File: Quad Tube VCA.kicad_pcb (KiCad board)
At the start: 2 copper layers, 162.6 x 100.3 mm, 226 parts, among them IC1 TL072, IC10 TL072, IC2 LM358, IC3 TL072, IC4 LM358, IC5 TL072, IC6 LM358, IC7 TL072, IC8 LM358, IC9 TL072

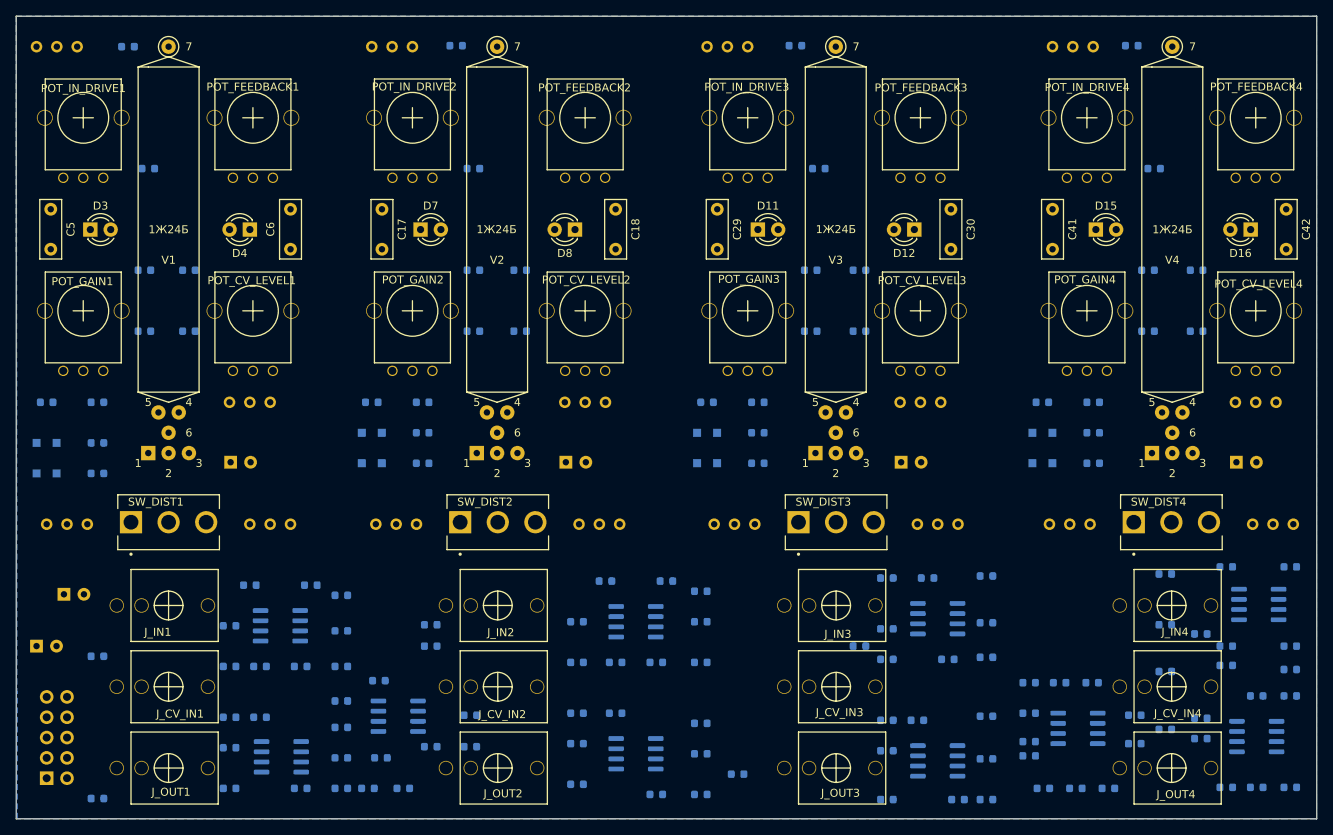
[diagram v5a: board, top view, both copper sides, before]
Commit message: first GND pour
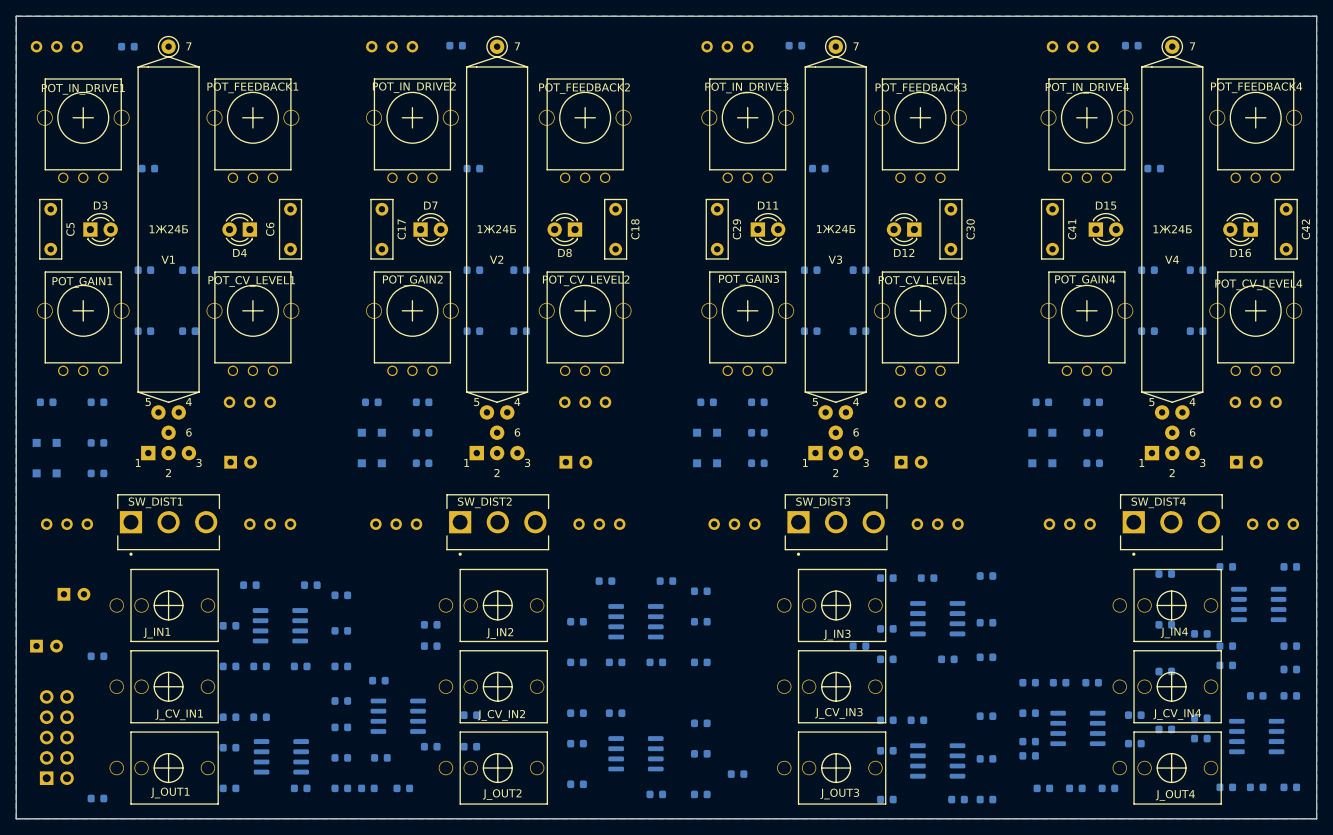
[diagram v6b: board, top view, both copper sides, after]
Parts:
- turned C16 to 180 degrees
- turned C46 to 180 degrees
- turned FB1 to 0 degrees
- turned R1 to 180 degrees
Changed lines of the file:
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@@
     (pad_to_mask_clearance 0.05)
     (aux_axis_origin 0 0)
-    (visible_elements FEFFF7FF)
+    (visible_elements FEFFFFFF)
     (pcbplotparams
       (layerselection 0x010fc_ffffffff)
@@
   )
   (module Resistor_SMD:R_0603_1608Metric (layer B.Cu)
-    (at 106.68 133.35)
+    (at 106.68 133.35 180)
     (descr "Resistor SMD 0603 (1608 Metric), square (rectangular) end terminal, IPC_7351 nominal, (Body size source: http://www.tortai-tech.com/upload/download/2011102023233369053.pdf), generated with kicad-footprint-generator")
     (tags resistor)
@@
       (effects (font (size 0.4 0.4) (thickness 0.06)) (justify mirror))
     )
-    (pad 2 smd roundrect (at 0.7875 0) (size 0.875 0.95) (layers B.Cu B.Paste B.Mask) (roundrect_rratio 0.25)
+    (pad 2 smd roundrect (at 0.7875 0 180) (size 0.875 0.95) (layers B.Cu B.Paste B.Mask) (roundrect_rratio 0.25)
       (net 81 "Net-(POT_FEEDBACK1-Pad1)"))
-    (pad 1 smd roundrect (at -0.7875 0) (size 0.875 0.95) (layers B.Cu B.Paste B.Mask) (roundrect_rratio 0.25)
+    (pad 1 smd roundrect (at -0.7875 0 180) (size 0.875 0.95) (layers B.Cu B.Paste B.Mask) (roundrect_rratio 0.25)
       (net 6 "Net-(C4-Pad2)"))
     (model ${KISYS3DMOD}/Resistor_SMD.3dshapes/R_0603_1608Metric.wrl
@@
   )
   (module Resistor_SMD:R_0603_1608Metric (layer B.Cu)
-    (at 76.2 142.24 180)
+    (at 76.2 142.24)
     (descr "Resistor SMD 0603 (1608 Metric), square (rectangular) end terminal, IPC_7351 nominal, (Body size source: http://www.tortai-tech.com/upload/download/2011102023233369053.pdf), generated with kicad-footprint-generator")
     (tags resistor)
@@
       (effects (font (size 0.4 0.4) (thickness 0.06)) (justify mirror))
     )
-    (pad 2 smd roundrect (at 0.7875 0 180) (size 0.875 0.95) (layers B.Cu B.Paste B.Mask) (roundrect_rratio 0.25)
+    (pad 2 smd roundrect (at 0.7875 0) (size 0.875 0.95) (layers B.Cu B.Paste B.Mask) (roundrect_rratio 0.25)
       (net 4 +12V))
-    (pad 1 smd roundrect (at -0.7875 0 180) (size 0.875 0.95) (layers B.Cu B.Paste B.Mask) (roundrect_rratio 0.25)
+    (pad 1 smd roundrect (at -0.7875 0) (size 0.875 0.95) (layers B.Cu B.Paste B.Mask) (roundrect_rratio 0.25)
       (net 127 "Net-(FB1-Pad1)"))
     (model ${KISYS3DMOD}/Resistor_SMD.3dshapes/R_0603_1608Metric.wrl
@@
   )
   (module Capacitor_SMD:C_0603_1608Metric (layer B.Cu)
-    (at 221.107 140.843)
+    (at 221.107 140.843 180)
     (descr "Capacitor SMD 0603 (1608 Metric), square (rectangular) end terminal, IPC_7351 nominal, (Body size source: http://www.tortai-tech.com/upload/download/2011102023233369053.pdf), generated with kicad-footprint-generator")
     (tags capacitor)
@@
       (effects (font (size 0.4 0.4) (thickness 0.06)) (justify mirror))
     )
-    (pad 2 smd roundrect (at 0.7875 0) (size 0.875 0.95) (layers B.Cu B.Paste B.Mask) (roundrect_rratio 0.25)
+    (pad 2 smd roundrect (at 0.7875 0 180) (size 0.875 0.95) (layers B.Cu B.Paste B.Mask) (roundrect_rratio 0.25)
       (net 3 GND))
-    (pad 1 smd roundrect (at -0.7875 0) (size 0.875 0.95) (layers B.Cu B.Paste B.Mask) (roundrect_rratio 0.25)
+    (pad 1 smd roundrect (at -0.7875 0 180) (size 0.875 0.95) (layers B.Cu B.Paste B.Mask) (roundrect_rratio 0.25)
       (net 4 +12V))
     (model ${KISYS3DMOD}/Capacitor_SMD.3dshapes/C_0603_1608Metric.wrl
@@
   )
   (module Capacitor_SMD:C_0603_1608Metric (layer B.Cu)
-    (at 156.21 139.192)
+    (at 156.21 139.192 180)
     (descr "Capacitor SMD 0603 (1608 Metric), square (rectangular) end terminal, IPC_7351 nominal, (Body size source: http://www.tortai-tech.com/upload/download/2011102023233369053.pdf), generated with kicad-footprint-generator")
     (tags capacitor)
@@
       (effects (font (size 0.4 0.4) (thickness 0.06)) (justify mirror))
     )
-    (pad 2 smd roundrect (at 0.7875 0) (size 0.875 0.95) (layers B.Cu B.Paste B.Mask) (roundrect_rratio 0.25)
+    (pad 2 smd roundrect (at 0.7875 0 180) (size 0.875 0.95) (layers B.Cu B.Paste B.Mask) (roundrect_rratio 0.25)
       (net 19 "Net-(C16-Pad2)"))
-    (pad 1 smd roundrect (at -0.7875 0) (size 0.875 0.95) (layers B.Cu B.Paste B.Mask) (roundrect_rratio 0.25)
+    (pad 1 smd roundrect (at -0.7875 0 180) (size 0.875 0.95) (layers B.Cu B.Paste B.Mask) (roundrect_rratio 0.25)
       (net 20 "Net-(C16-Pad1)"))
     (model ${KISYS3DMOD}/Capacitor_SMD.3dshapes/C_0603_1608Metric.wrl
@@
     (polygon
       (pts
-        (xy 228.6 144.78) (xy 66.167 144.78) (xy 66.04 44.577) (xy 66.04 44.45) (xy 228.6 44.45)
+        (xy 228.6 144.78) (xy 66.04 144.78) (xy 66.04 44.45) (xy 228.6 44.45)
       )
     )

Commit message: +12V net
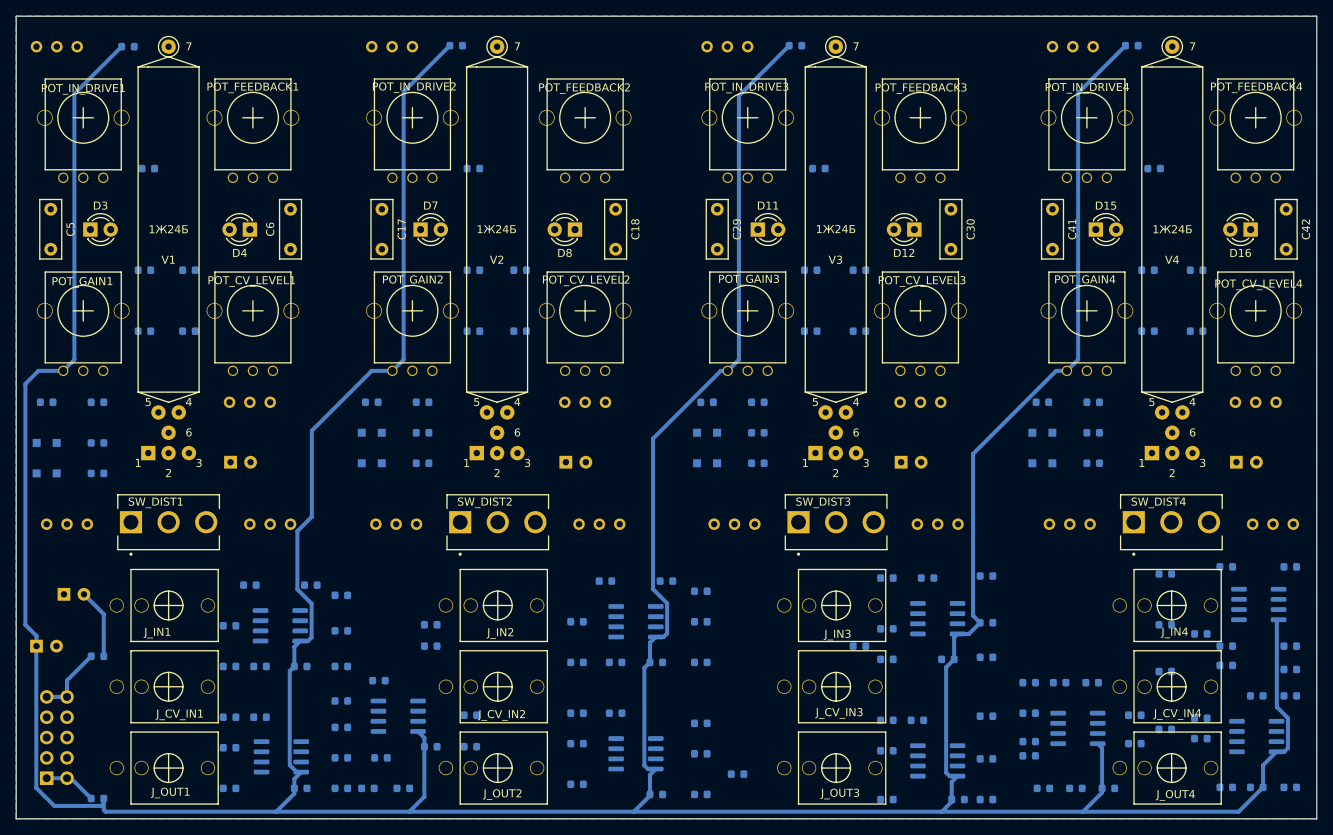
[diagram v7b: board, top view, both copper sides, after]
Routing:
- net +12V: track 0.00 -> 629.5 mm
- net Net-(FB2-Pad1): track 0.00 -> 8.87 mm
- net -12V: track 0.00 -> 8.77 mm
- net Net-(FB1-Pad1): track 0.00 -> 6.61 mm

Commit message: -12V net
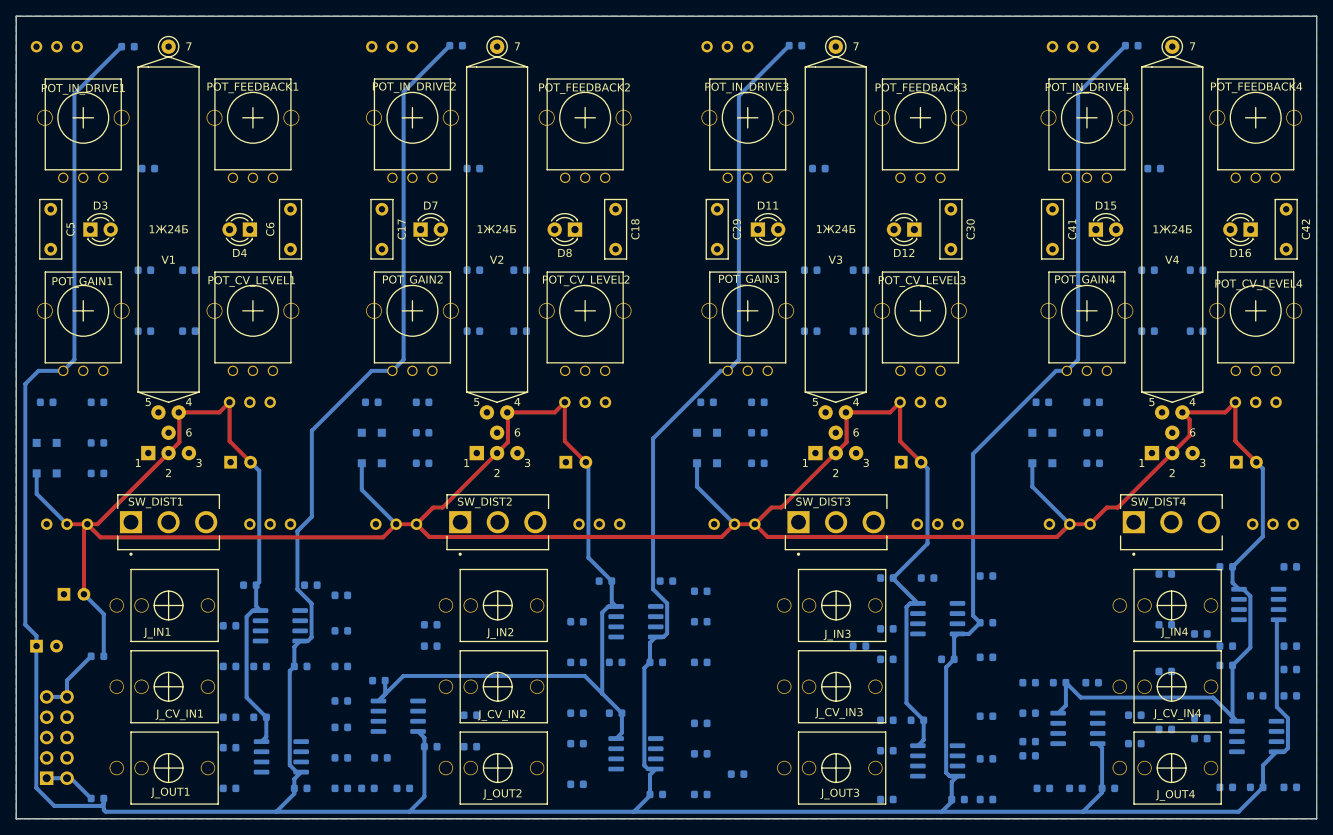
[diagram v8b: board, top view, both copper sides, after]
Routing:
- net -12V: track 8.77 -> 543.7 mm
